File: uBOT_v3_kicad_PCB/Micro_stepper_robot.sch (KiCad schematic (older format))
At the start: 8 parts, among them J1 Conn_01x04_Male, J2 Conn_01x04_Male, J3 Conn_01x04_Male, J4 Conn_01x04_Male, M1 Stepper_Motor_bipolar, M2 Stepper_Motor_bipolar, M3 Stepper_Motor_bipolar, M4 Stepper_Motor_bipolar

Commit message: started v3 circuit design
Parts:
- removed J1, J2, J3, J4: Conn_01x04_Male, Connector_PinHeader_2.54mm:PinHeader_1x04_P2.54mm_Vertical, symbol Connector:Conn_01x04_Male
- removed M2, M3, M4: Stepper_Motor_bipolar, kicad_footprints:micro_stepper1, symbol Motor:Stepper_Motor_bipolar
- added BT?: Battery_Cell, symbol Device:Battery_Cell
- added J?: USB_B_Mini, symbol Connector:USB_B_Mini
- added M? (x3): Stepper_Motor_bipolar, kicad_footprints:micro_stepper1, symbol Motor:Stepper_Motor_bipolar
- added U?: ATmega328-PU, Package_DIP:DIP-28_W7.62mm, symbol MCU_Microchip_ATmega:ATmega328-PU
- added U?: MCP73812T-420I-OT, Package_TO_SOT_SMD:SOT-23-5, symbol Battery_Management:MCP73812T-420I-OT
- added U?: FT231XS, Package_SO:SSOP-20_3.9x8.7mm_P0.635mm, symbol Interface_USB:FT231XS
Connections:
- wire segments 44 -> 0
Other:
- moved on the sheet: M1
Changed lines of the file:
@@
 L Motor:Stepper_Motor_bipolar M1
 U 1 1 5E6E63B8
-P 4100 3050
-F 0 "M1" H 4288 3173 50  0000 L CNN
-F 1 "Stepper_Motor_bipolar" H 4288 3082 50  0000 L CNN
-F 2 "kicad_footprints:micro_stepper1" H 4110 3040 50  0001 C CNN
-F 3 "http://www.infineon.com/dgdl/Application-Note-TLE8110EE_driving_UniPolarStepperMotor_V1.1.pdf?fileId=db3a30431be39b97011be5d0aa0a00b0" H 4110 3040 50  0001 C CNN
-	1    4100 3050
+P 9750 3050
+F 0 "M1" H 9938 3173 50  0000 L CNN
+F 1 "Stepper_Motor_bipolar" H 9938 3082 50  0000 L CNN
+F 2 "kicad_footprints:micro_stepper1" H 9760 3040 50  0001 C CNN
+F 3 "http://www.infineon.com/dgdl/Application-Note-TLE8110EE_driving_UniPolarStepperMotor_V1.1.pdf?fileId=db3a30431be39b97011be5d0aa0a00b0" H 9760 3040 50  0001 C CNN
+	1    9750 3050
 	1    0    0    -1
 $EndComp
 $Comp
-L Connector:Conn_01x04_Male J1
-U 1 1 5E6F69D0
-P 4100 2300
-F 0 "J1" V 4160 2440 50  0000 L CNN
-F 1 "Conn_01x04_Male" V 4251 2440 50  0000 L CNN
-F 2 "Connector_PinHeader_2.54mm:PinHeader_1x04_P2.54mm_Vertical" H 4100 2300 50  0001 C CNN
-F 3 "~" H 4100 2300 50  0001 C CNN
-	1    4100 2300
-	0    1    1    0
-$EndComp
-Wire Wire Line
-	4200 2500 4200 2750
-Wire Wire Line
-	4100 2500 4100 2750
-Wire Wire Line
-	4100 2750 4000 2750
-Wire Wire Line
-	4000 2500 4000 2700
-Wire Wire Line
-	4000 2700 3750 2700
-Wire Wire Line
-	3750 2700 3750 2950
-Wire Wire Line
-	3750 2950 3800 2950
-Wire Wire Line
-	3900 2500 3900 2650
-Wire Wire Line
-	3900 2650 3700 2650
-Wire Wire Line
-	3700 2650 3700 3150
-Wire Wire Line
-	3700 3150 3800 3150
-$Comp
-L Motor:Stepper_Motor_bipolar M3
-U 1 1 5E6F7092
-P 6850 3150
-F 0 "M3" H 7038 3273 50  0000 L CNN
-F 1 "Stepper_Motor_bipolar" H 7038 3182 50  0000 L CNN
-F 2 "kicad_footprints:micro_stepper1" H 6860 3140 50  0001 C CNN
-F 3 "http://www.infineon.com/dgdl/Application-Note-TLE8110EE_driving_UniPolarStepperMotor_V1.1.pdf?fileId=db3a30431be39b97011be5d0aa0a00b0" H 6860 3140 50  0001 C CNN
-	1    6850 3150
+L Motor:Stepper_Motor_bipolar M?
+U 1 1 5EF0ADEA
+P 9750 3650
+F 0 "M?" H 9938 3773 50  0000 L CNN
+F 1 "Stepper_Motor_bipolar" H 9938 3682 50  0000 L CNN
+F 2 "kicad_footprints:micro_stepper1" H 9760 3640 50  0001 C CNN
+F 3 "http://www.infineon.com/dgdl/Application-Note-TLE8110EE_driving_UniPolarStepperMotor_V1.1.pdf?fileId=db3a30431be39b97011be5d0aa0a00b0" H 9760 3640 50  0001 C CNN
+	1    9750 3650
 	1    0    0    -1
 $EndComp
 $Comp
-L Connector:Conn_01x04_Male J3
-U 1 1 5E6F7098
-P 6850 2400
-F 0 "J3" V 6910 2540 50  0000 L CNN
-F 1 "Conn_01x04_Male" V 7001 2540 50  0000 L CNN
-F 2 "Connector_PinHeader_2.54mm:PinHeader_1x04_P2.54mm_Vertical" H 6850 2400 50  0001 C CNN
-F 3 "~" H 6850 2400 50  0001 C CNN
-	1    6850 2400
-	0    1    1    0
-$EndComp
-Wire Wire Line
-	6950 2600 6950 2850
-Wire Wire Line
-	6850 2600 6850 2850
-Wire Wire Line
-	6850 2850 6750 2850
-Wire Wire Line
-	6750 2600 6750 2800
-Wire Wire Line
-	6750 2800 6500 2800
-Wire Wire Line
-	6500 2800 6500 3050
-Wire Wire Line
-	6500 3050 6550 3050
-Wire Wire Line
-	6650 2600 6650 2750
-Wire Wire Line
-	6650 2750 6450 2750
-Wire Wire Line
-	6450 2750 6450 3250
-Wire Wire Line
-	6450 3250 6550 3250
-$Comp
-L Motor:Stepper_Motor_bipolar M2
-U 1 1 5E6F7332
-P 4150 4350
-F 0 "M2" H 4338 4473 50  0000 L CNN
-F 1 "Stepper_Motor_bipolar" H 4338 4382 50  0000 L CNN
-F 2 "kicad_footprints:micro_stepper1" H 4160 4340 50  0001 C CNN
-F 3 "http://www.infineon.com/dgdl/Application-Note-TLE8110EE_driving_UniPolarStepperMotor_V1.1.pdf?fileId=db3a30431be39b97011be5d0aa0a00b0" H 4160 4340 50  0001 C CNN
-	1    4150 4350
+L Motor:Stepper_Motor_bipolar M?
+U 1 1 5EF0B15F
+P 9750 4200
+F 0 "M?" H 9938 4323 50  0000 L CNN
+F 1 "Stepper_Motor_bipolar" H 9938 4232 50  0000 L CNN
+F 2 "kicad_footprints:micro_stepper1" H 9760 4190 50  0001 C CNN
+F 3 "http://www.infineon.com/dgdl/Application-Note-TLE8110EE_driving_UniPolarStepperMotor_V1.1.pdf?fileId=db3a30431be39b97011be5d0aa0a00b0" H 9760 4190 50  0001 C CNN
+	1    9750 4200
 	1    0    0    -1
 $EndComp
 $Comp
-L Connector:Conn_01x04_Male J2
-U 1 1 5E6F7338
-P 4150 3600
-F 0 "J2" V 4210 3740 50  0000 L CNN
-F 1 "Conn_01x04_Male" V 4301 3740 50  0000 L CNN
-F 2 "Connector_PinHeader_2.54mm:PinHeader_1x04_P2.54mm_Vertical" H 4150 3600 50  0001 C CNN
-F 3 "~" H 4150 3600 50  0001 C CNN
-	1    4150 3600
-	0    1    1    0
-$EndComp
-Wire Wire Line
-	4250 3800 4250 4050
-Wire Wire Line
-	4150 3800 4150 4050
-Wire Wire Line
-	4150 4050 4050 4050
-Wire Wire Line
-	4050 3800 4050 4000
-Wire Wire Line
-	4050 4000 3800 4000
-Wire Wire Line
-	3800 4000 3800 4250
-Wire Wire Line
-	3800 4250 3850 4250
-Wire Wire Line
-	3950 3800 3950 3950
-Wire Wire Line
-	3950 3950 3750 3950
-Wire Wire Line
-	3750 3950 3750 4450
-Wire Wire Line
-	3750 4450 3850 4450
-$Comp
-L Motor:Stepper_Motor_bipolar M4
-U 1 1 5E6F78BF
-P 6850 4400
-F 0 "M4" H 7038 4523 50  0000 L CNN
-F 1 "Stepper_Motor_bipolar" H 7038 4432 50  0000 L CNN
-F 2 "kicad_footprints:micro_stepper1" H 6860 4390 50  0001 C CNN
-F 3 "http://www.infineon.com/dgdl/Application-Note-TLE8110EE_driving_UniPolarStepperMotor_V1.1.pdf?fileId=db3a30431be39b97011be5d0aa0a00b0" H 6860 4390 50  0001 C CNN
-	1    6850 4400
+L Motor:Stepper_Motor_bipolar M?
+U 1 1 5EF0B559
+P 9750 4750
+F 0 "M?" H 9938 4873 50  0000 L CNN
+F 1 "Stepper_Motor_bipolar" H 9938 4782 50  0000 L CNN
+F 2 "kicad_footprints:micro_stepper1" H 9760 4740 50  0001 C CNN
+F 3 "http://www.infineon.com/dgdl/Application-Note-TLE8110EE_driving_UniPolarStepperMotor_V1.1.pdf?fileId=db3a30431be39b97011be5d0aa0a00b0" H 9760 4740 50  0001 C CNN
+	1    9750 4750
 	1    0    0    -1
 $EndComp
 $Comp
-L Connector:Conn_01x04_Male J4
-U 1 1 5E6F78C5
-P 6850 3650
-F 0 "J4" V 6910 3790 50  0000 L CNN
-F 1 "Conn_01x04_Male" V 7001 3790 50  0000 L CNN
-F 2 "Connector_PinHeader_2.54mm:PinHeader_1x04_P2.54mm_Vertical" H 6850 3650 50  0001 C CNN
-F 3 "~" H 6850 3650 50  0001 C CNN
-	1    6850 3650
-	0    1    1    0
+L MCU_Microchip_ATmega:ATmega328-PU U?
+U 1 1 5EF0E4CA
+P 2200 3950
+F 0 "U?" H 1556 3996 50  0000 R CNN
+F 1 "ATmega328-PU" H 1556 3905 50  0000 R CNN
+F 2 "Package_DIP:DIP-28_W7.62mm" H 2200 3950 50  0001 C CIN
+F 3 "http://ww1.microchip.com/downloads/en/DeviceDoc/ATmega328_P%20AVR%20MCU%20with%20picoPower%20Technology%20Data%20Sheet%2040001984A.pdf" H 2200 3950 50  0001 C CNN
+	1    2200 3950
+	1    0    0    -1
 $EndComp
-Wire Wire Line
-	6950 3850 6950 4100
-Wire Wire Line
-	6850 3850 6850 4100
-Wire Wire Line
-	6850 4100 6750 4100
-Wire Wire Line
-	6750 3850 6750 4050
-Wire Wire Line
-	6750 4050 6500 4050
-Wire Wire Line
-	6500 4050 6500 4300
-Wire Wire Line
-	6500 4300 6550 4300
-Wire Wire Line
-	6650 3850 6650 4000
-Wire Wire Line
-	6650 4000 6450 4000
-Wire Wire Line
-	6450 4000 6450 4500
-Wire Wire Line
-	6450 4500 6550 4500
+$Comp
+L Battery_Management:MCP73812T-420I-OT U?
+U 1 1 5EF0FBE9
+P 5100 1450
+F 0 "U?" H 5544 1496 50  0000 L CNN
+F 1 "MCP73812T-420I-OT" H 5544 1405 50  0000 L CNN
+F 2 "Package_TO_SOT_SMD:SOT-23-5" H 5150 1200 50  0001 L CNN
+F 3 "http://ww1.microchip.com/downloads/en/DeviceDoc/22036b.pdf" H 4850 1700 50  0001 C CNN
+	1    5100 1450
+	1    0    0    -1
+$EndComp
+$Comp
+L Device:Battery_Cell BT?
+U 1 1 5EF109A6
+P 3500 1400
+F 0 "BT?" H 3618 1496 50  0000 L CNN
+F 1 "Battery_Cell" H 3618 1405 50  0000 L CNN
+F 2 "" V 3500 1460 50  0001 C CNN
+F 3 "~" V 3500 1460 50  0001 C CNN
+	1    3500 1400
+	1    0    0    -1
+$EndComp
+$Comp
+L Connector:USB_B_Mini J?
+U 1 1 5EF118EB
+P 7850 1600
+F 0 "J?" H 7907 2067 50  0000 C CNN
+F 1 "USB_B_Mini" H 7907 1976 50  0000 C CNN
+F 2 "" H 8000 1550 50  0001 C CNN
+F 3 "~" H 8000 1550 50  0001 C CNN
+	1    7850 1600
+	1    0    0    -1
+$EndComp
+$Comp
+L Interface_USB:FT231XS U?
+U 1 1 5EF17383
+P 5800 3750
+F 0 "U?" H 5800 4831 50  0000 C CNN
+F 1 "FT231XS" H 5800 4740 50  0000 C CNN
+F 2 "Package_SO:SSOP-20_3.9x8.7mm_P0.635mm" H 6800 2950 50  0001 C CNN
+F 3 "https://www.ftdichip.com/Support/Documents/DataSheets/ICs/DS_FT231X.pdf" H 5800 3750 50  0001 C CNN
+	1    5800 3750
+	1    0    0    -1
+$EndComp
 $EndSCHEMATC

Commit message: added h bridge drivers
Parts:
- removed U?: ATmega328-PU, Package_DIP:DIP-28_W7.62mm, symbol MCU_Microchip_ATmega:ATmega328-PU
- added U?: ESP32-WROOM-32, RF_Module:ESP32-WROOM-32, symbol RF_Module:ESP32-WROOM-32
- added U?: LM1117-3.3, symbol Regulator_Linear:LM1117-3.3
- added U? (x2): DRV8833PW, Package_SO:TSSOP-16_4.4x5mm_P0.65mm, symbol Driver_Motor:DRV8833PW
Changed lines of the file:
@@
-$EndComp
-$Comp
-L MCU_Microchip_ATmega:ATmega328-PU U?
-U 1 1 5EF0E4CA
-P 2200 3950
-F 0 "U?" H 1556 3996 50  0000 R CNN
-F 1 "ATmega328-PU" H 1556 3905 50  0000 R CNN
-F 2 "Package_DIP:DIP-28_W7.62mm" H 2200 3950 50  0001 C CIN
-F 3 "http://ww1.microchip.com/downloads/en/DeviceDoc/ATmega328_P%20AVR%20MCU%20with%20picoPower%20Technology%20Data%20Sheet%2040001984A.pdf" H 2200 3950 50  0001 C CNN
-	1    2200 3950
-	1    0    0    -1
 $EndComp
 $Comp
@@
 	1    0    0    -1
 $EndComp
+$Comp
+L RF_Module:ESP32-WROOM-32 U?
+U 1 1 5EF0D093
+P 2600 3950
+F 0 "U?" H 2600 5531 50  0000 C CNN
+F 1 "ESP32-WROOM-32" H 2600 5440 50  0000 C CNN
+F 2 "RF_Module:ESP32-WROOM-32" H 2600 2450 50  0001 C CNN
+F 3 "https://www.espressif.com/sites/default/files/documentation/esp32-wroom-32_datasheet_en.pdf" H 2300 4000 50  0001 C CNN
+	1    2600 3950
+	1    0    0    -1
+$EndComp
+$Comp
+L Regulator_Linear:LM1117-3.3 U?
+U 1 1 5EF11066
+P 7100 1300
+F 0 "U?" H 7100 1542 50  0000 C CNN
+F 1 "LM1117-3.3" H 7100 1451 50  0000 C CNN
+F 2 "" H 7100 1300 50  0001 C CNN
+F 3 "http://www.ti.com/lit/ds/symlink/lm1117.pdf" H 7100 1300 50  0001 C CNN
+	1    7100 1300
+	1    0    0    -1
+$EndComp
+$Comp
+L Driver_Motor:DRV8833PW U?
+U 1 1 5EF13196
+P 8050 3200
+F 0 "U?" H 8050 2411 50  0000 C CNN
+F 1 "DRV8833PW" H 8050 2320 50  0000 C CNN
+F 2 "Package_SO:TSSOP-16_4.4x5mm_P0.65mm" H 8500 3650 50  0001 L CNN
+F 3 "http://www.ti.com/lit/ds/symlink/drv8833.pdf" H 7900 3750 50  0001 C CNN
+	1    8050 3200
+	1    0    0    -1
+$EndComp
+$Comp
+L Driver_Motor:DRV8833PW U?
+U 1 1 5EF140EA
+P 8050 5100
+F 0 "U?" H 8050 4311 50  0000 C CNN
+F 1 "DRV8833PW" H 8050 4220 50  0000 C CNN
+F 2 "Package_SO:TSSOP-16_4.4x5mm_P0.65mm" H 8500 5550 50  0001 L CNN
+F 3 "http://www.ti.com/lit/ds/symlink/drv8833.pdf" H 7900 5650 50  0001 C CNN
+	1    8050 5100
+	1    0    0    -1
+$EndComp

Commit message: progressed schematic
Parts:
- added R? (x2): 27R, symbol Device:R_Small
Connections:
- net GND: now reaches U?.1 (GND), U?.15 (GND), U?.38 (GND), U?.39 (GND)
- net GND: now also BT?.2 (-), J?.5 (GND), J?.6 (Shield), U?.1 (GND), U?.16 (GND), U?.2 (VSS), U?.6 (GND)
- net +3V3: now reaches U?.2 (VDD)
- net +3V3: now also U?.13 (3V3OUT), U?.15 (VCC), U?.2 (VO), U?.3 (VCCIO)
- net +BATT: now reaches U?.3 (VBAT)
- net +BATT: now also BT?.1 (+), U?.3 (VI)
- net +5V: now reaches U?.4 (VDD)
- net +5V: now also J?.1 (VBUS)
- net at J?.2 (D-): now also R?.2
- net at J?.3 (D+): now also R?.2
- net USB_D+: now reaches U?.11 (USBDP)
- net USB_D+: now also R?.1
- net USB_D-: now reaches U?.12 (USBDM)
- net USB_D-: now also R?.1
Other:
- moved on the sheet: J?, U?

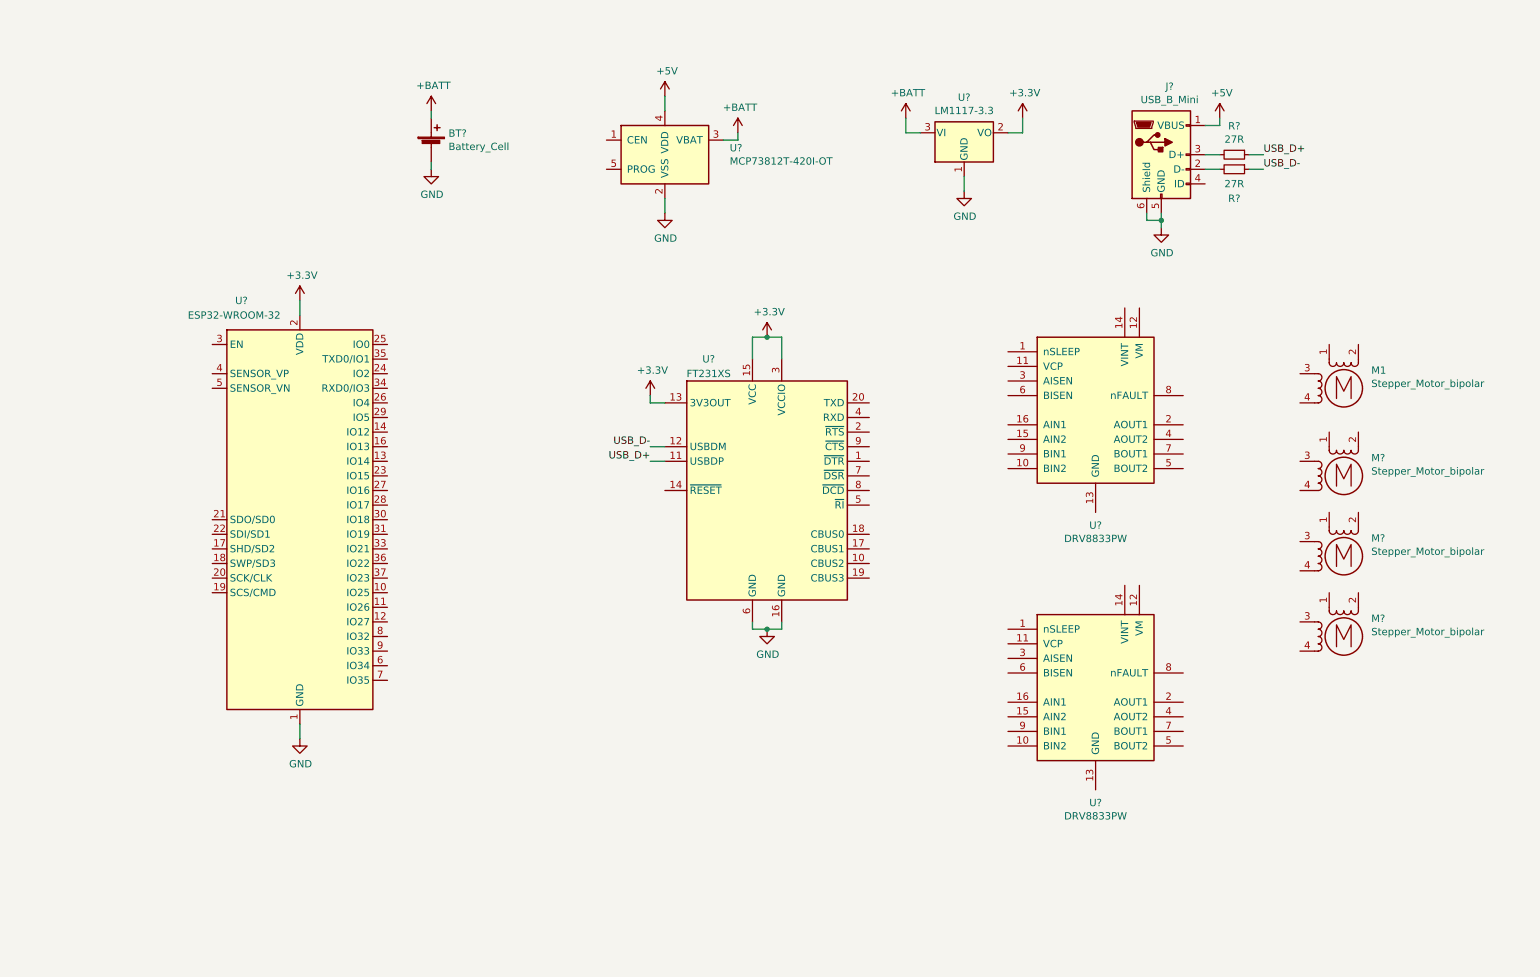
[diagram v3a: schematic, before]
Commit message: started stepper motor schematic
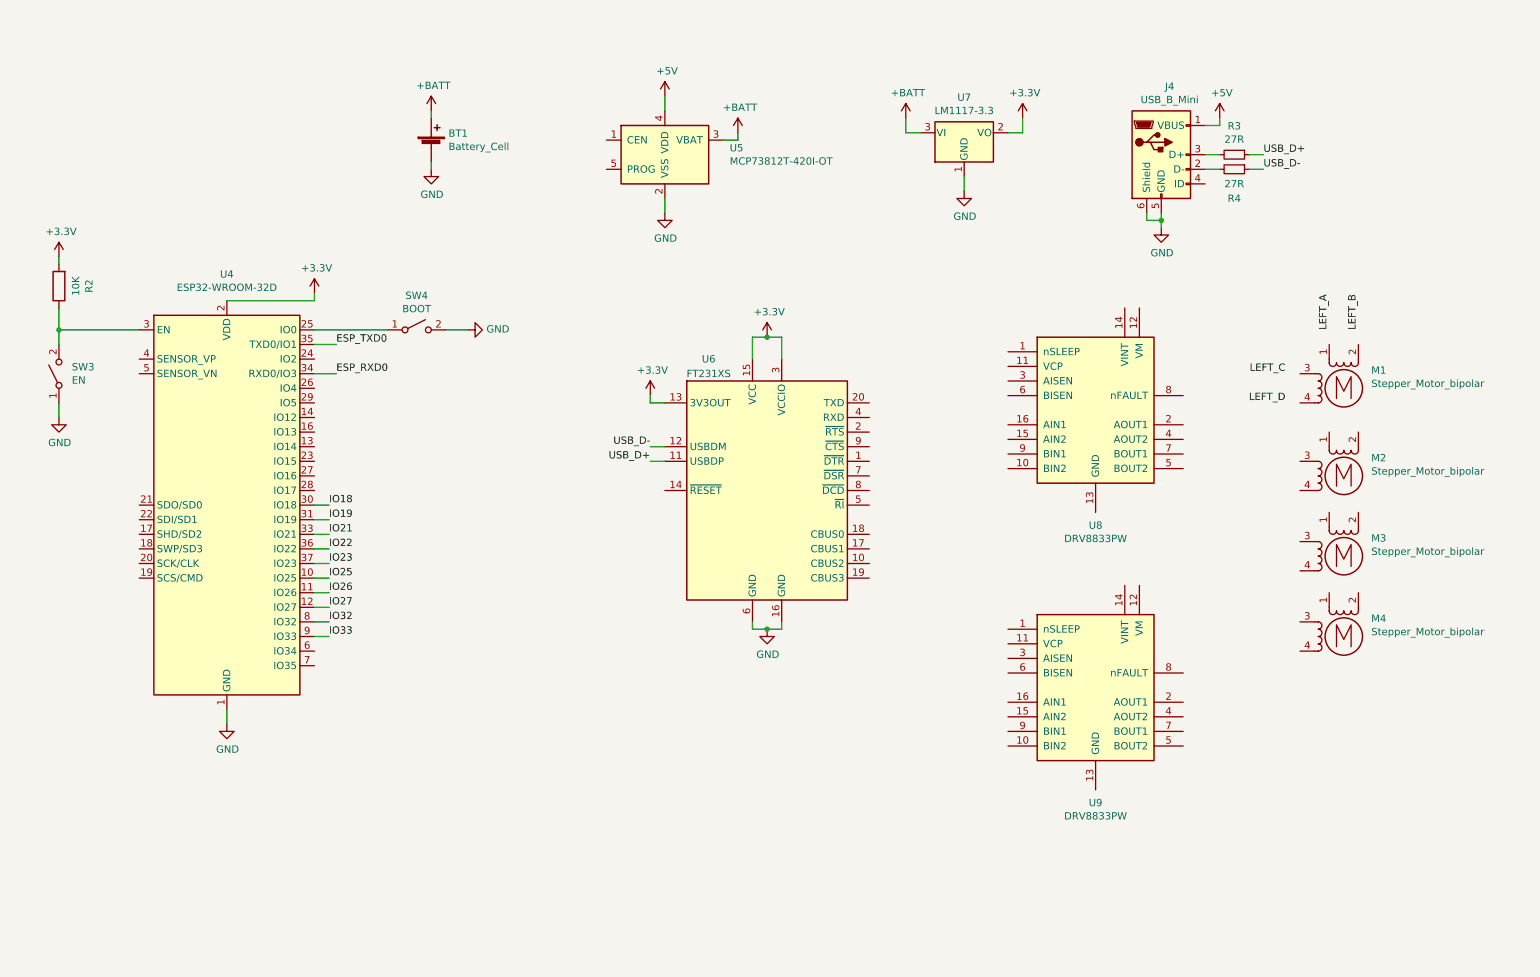
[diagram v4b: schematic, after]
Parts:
- removed U?: ESP32-WROOM-32, RF_Module:ESP32-WROOM-32, symbol RF_Module:ESP32-WROOM-32
- added R2: 10K, Resistor_SMD:R_0805_2012Metric, symbol Device:R
- added SW3: EN, Button_Switch_SMD:SW_SPST_B3U-1000P, symbol Switch:SW_SPST
- added SW4: BOOT, Button_Switch_SMD:SW_SPST_B3U-1000P, symbol Switch:SW_SPST
- added U4: ESP32-WROOM-32D, RF_Module:ESP32-WROOM-32, symbol RF_Module:ESP32-WROOM-32D
- gave numbers to parts that had none: 12
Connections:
- net +3V3: now also R2.2, U4.2 (VDD)
- net GND: now also SW3.1 (A), SW4.2 (B), U4.1 (GND), U4.15 (GND), U4.38 (GND), U4.39 (GND)
- new net: SW4.1 (A), U4.25 (IO0)
- new net: R2.1, SW3.2 (B), U4.3 (EN)
- new net ESP_RXD0: U4.34 (RXD0/IO3)
- new net ESP_TXD0: U4.35 (TXD0/IO1)
- new net IO18: U4.30 (IO18)
- new net IO19: U4.31 (IO19)
- new net IO21: U4.33 (IO21)
- new net IO22: U4.36 (IO22)
- new net IO23: U4.37 (IO23)
- new net IO25: U4.10 (IO25)
- new net IO26: U4.11 (IO26)
- new net IO27: U4.12 (IO27)
- new net IO32: U4.8 (IO32)
- new net IO33: U4.9 (IO33)

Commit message: added tcrt5000
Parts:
- removed U8: DRV8833PW, Package_SO:TSSOP-16_4.4x5mm_P0.65mm, symbol Driver_Motor:DRV8833PW
- added C1, C2: 0.01uF, symbol Device:C_Small
- added C3, C4: C_Small, symbol Device:C_Small
- added C5, C6: 4.7uF, symbol Device:C_Small
- added D1: LED_Small, symbol Device:LED_Small
- added R1: 10k, symbol Device:R_Small
- added R5, R6: 220R, symbol Device:R_Small
- added R7: 2k, symbol Device:R_Small
- added U1: DRV8833PW, Package_SO:TSSOP-16_4.4x5mm_P0.65mm, symbol Driver_Motor:DRV8833PW
- added U2: TCRT5000, OPTO_TCRT5000, symbol Kicad_symbols:TCRT5000
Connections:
- net IO19 is gone; now on net LEFT_A_IO: U4.31 (IO19)
- net IO21 is gone; now on net LEFT_B_IO: U4.33 (IO21)
- net IO22 is gone; now on net LEFT_C_IO: U4.36 (IO22)
- net IO23 is gone; now on net LEFT_D_IO: U4.37 (IO23)
- net +3V3: now also U2.A, U2.COLL
- net +5V: now also C5.1, D1.2 (A)
- net +BATT: now also U9.12 (VM), C1.2, C2.2, C6.1, U1.12 (VM)
- net GND: now also U9.13 (GND), U9.3 (AISEN), U9.6 (BISEN), C3.2, C4.2, C5.2, C6.2, R1.2, R5.2, R7.2, U1.13 (GND), U1.3 (AISEN), U1.6 (BISEN)
- net LEFT_A: now also M1.1, M2.1, U9.2 (AOUT1)
- net LEFT_B: now also M1.2 (-), M2.2 (-), U9.4 (AOUT2)
- net LEFT_C: now also M1.3, M2.3, U9.7 (BOUT1)
- net LEFT_D: now also M1.4, M2.4, U9.5 (BOUT2)
- net RIGHT_A: now reaches M3.1
- net RIGHT_A: now also M4.1, U1.2 (AOUT1)
- net RIGHT_B: now reaches M3.2 (-)
- net RIGHT_B: now also M4.2 (-), U1.4 (AOUT2)
- net RIGHT_C: now reaches M3.3
- net RIGHT_C: now also M4.3, U1.7 (BOUT1)
- net RIGHT_D: now reaches M3.4
- net RIGHT_D: now also M4.4, U1.5 (BOUT2)
- net at U5.1 (CEN): now also R6.2
- net at U5.5 (PROG): now also R7.1
- net MOTOR_SLEEP: now reaches U9.1 (nSLEEP)
- net MOTOR_SLEEP: now also U4.27 (IO16), U1.1 (nSLEEP)
- net LEFT_D_IO: now reaches U9.10 (BIN2)
- net at U9.11 (VCP): now also C2.1
- net at U9.14 (VINT): now also C4.1
- net LEFT_B_IO: now reaches U9.15 (AIN2)
- net LEFT_A_IO: now reaches U9.16 (AIN1)
- net LEFT_FAULT: now reaches U9.8 (nFAULT)
- net LEFT_FAULT: now also U4.28 (IO17)
- net LEFT_C_IO: now reaches U9.9 (BIN1)
- net IR_VOUT: now reaches U4.6 (IO34)
- net IR_VOUT: now also R1.1, U2.CATH
- net IO18 renamed RIGHT_FAULT
- net RIGHT_FAULT: now also U1.8 (nFAULT)
- net IO25 renamed RIGHT_A_IO
- net RIGHT_A_IO: now also U1.16 (AIN1)
- net IO26 renamed RIGHT_B_IO
- net RIGHT_B_IO: now also U1.15 (AIN2)
- net IO27 renamed RIGHT_C_IO
- net RIGHT_C_IO: now also U1.9 (BIN1)
- net IO32 renamed RIGHT_D_IO
- net RIGHT_D_IO: now also U1.10 (BIN2)
- net IO33: no longer names the net of U4.9 (IO33)
- new net: C1.1, U1.11 (VCP)
- new net: C3.1, U1.14 (VINT)
- new net: R5.1, U2.E
- new net: D1.1 (K), R6.1
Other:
- note added: "LEFT MOTORS"
- note added: "LEFT SIDE MOTORS"
- note added: "RIGHT MOTORS"
- note added: "RIGHT SIDE MOTORS"
- moved on the sheet: BT1, J4, M1, M2, M3, M4, R3, R4, U5, U7, U9
